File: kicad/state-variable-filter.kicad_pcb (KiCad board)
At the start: 2 copper layers, 0 parts

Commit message: Updating hardware design
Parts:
- added C1: 10nF, Rumblesan_Standard_Parts:C_Rect_L7.0mm_W2.5mm_P5.00mm, F.Cu at (127.6, 58.7)
- added C10: 100nF, Rumblesan_Standard_Parts:C_Rect_L7.0mm_W2.5mm_P5.00mm, F.Cu at (154.4, 52.8)
- added C11: 22pF, Rumblesan_Standard_Parts:C_Rect_L7.0mm_W2.5mm_P5.00mm, F.Cu at (140.2, 58.7)
- added C12: 220pF, Capacitor_THT:C_Rect_L7.0mm_W4.5mm_P5.00mm, F.Cu at (152.7, 88.4)
- added C13: 100nF, Rumblesan_Standard_Parts:C_Rect_L7.0mm_W2.5mm_P5.00mm, F.Cu at (151.4, 85.3)
- added C14: 22pF, Rumblesan_Standard_Parts:C_Rect_L7.0mm_W2.5mm_P5.00mm, F.Cu at (156.7, 71.6)
- added C15: 560pF, Rumblesan_Standard_Parts:C_Rect_L7.0mm_W2.5mm_P5.00mm, F.Cu at (161.5, 97.3)
- added C16: 100nF, Rumblesan_Standard_Parts:C_Rect_L7.0mm_W2.5mm_P5.00mm, F.Cu at (151.4, 134.4)
- added C17: 560pF, Rumblesan_Standard_Parts:C_Rect_L7.0mm_W2.5mm_P5.00mm, F.Cu at (161.0, 117.3)
- added C18: 22pF, Rumblesan_Standard_Parts:C_Rect_L7.0mm_W2.5mm_P5.00mm, F.Cu at (164.1, 126.2)
- added C19: 10uF, Rumblesan_Standard_Parts:CP_Radial_D5.0mm_P2.00mm, B.Cu at (162.6, 153.4)
- added C2: 100nF, Rumblesan_Standard_Parts:C_Rect_L7.0mm_W2.5mm_P5.00mm, F.Cu at (135.2, 61.7)
- added C20: 10uF, Rumblesan_Standard_Parts:CP_Radial_D5.0mm_P2.00mm, B.Cu at (123.2, 153.4)
- added C3: 100nF, Rumblesan_Standard_Parts:C_Rect_L7.0mm_W2.5mm_P5.00mm, F.Cu at (132.2, 85.3)
- added C4: 220pF, Capacitor_THT:C_Rect_L7.0mm_W4.5mm_P5.00mm, F.Cu at (135.9, 88.4)
- added C5: 560pF, Rumblesan_Standard_Parts:C_Rect_L7.0mm_W2.5mm_P5.00mm, F.Cu at (133.9, 106.9)
- added C6: 100nF, Rumblesan_Standard_Parts:C_Rect_L7.0mm_W2.5mm_P5.00mm, F.Cu at (132.2, 101.9)
- added C7: 100nF, Rumblesan_Standard_Parts:C_Rect_L7.0mm_W2.5mm_P5.00mm, F.Cu at (137.2, 120.1)
- added C8: 100nF, Rumblesan_Standard_Parts:C_Rect_L7.0mm_W2.5mm_P5.00mm, F.Cu at (132.2, 135.9)
- added C9: 20pF, Rumblesan_Standard_Parts:C_Rect_L7.0mm_W2.5mm_P5.00mm, F.Cu at (122.3, 132.8)
- added D1: 1N4148, Rumblesan_Standard_Parts:D_DO-35_SOD27_P7.62mm_Horizontal, F.Cu at (132.8, 61.5)
- added D10: 1N4148, Rumblesan_Standard_Parts:D_DO-35_SOD27_P7.62mm_Horizontal, F.Cu at (151.1, 128.5)
- added D11: 1N5818, Rumblesan_Standard_Parts:D_DO-41_SOD81_P10.16mm_Horizontal, F.Cu at (157.0, 147.6)
- added D2: 1N4148, Rumblesan_Standard_Parts:D_DO-35_SOD27_P7.62mm_Horizontal, F.Cu at (133.6, 67.6)
- added D3: 1n4148, Rumblesan_Standard_Parts:D_DO-35_SOD27_P7.62mm_Horizontal, F.Cu at (129.8, 133.1)
- added D4: 1n4148, Rumblesan_Standard_Parts:D_DO-35_SOD27_P7.62mm_Horizontal, F.Cu at (129.8, 136.1)
- added D5: 1N5818, Rumblesan_Standard_Parts:D_DO-41_SOD81_P10.16mm_Horizontal, F.Cu at (129.0, 157.7)
- added D6: 1N4148, Rumblesan_Standard_Parts:D_DO-35_SOD27_P7.62mm_Horizontal, F.Cu at (140.5, 55.9)
- added D7: 6v8, Rumblesan_Standard_Parts:D_DO-35_SOD27_P7.62mm_Horizontal, F.Cu at (161.3, 108.5)
- added D8: 6v8, Rumblesan_Standard_Parts:D_DO-35_SOD27_P7.62mm_Horizontal, F.Cu at (158.8, 98.3)
- added D9: 1N4148, Rumblesan_Standard_Parts:D_DO-35_SOD27_P7.62mm_Horizontal, F.Cu at (158.8, 126.0)
- added J1: AudioJack2_SwitchT, Rumblesan_Audio_Connectors:Jack_3.5mm_QingPu_WQP-PJ398SM_Vertical, F.Cu at (81.5, 58.0)
- added J10: AudioJack2_SwitchT, Rumblesan_Audio_Connectors:Jack_3.5mm_QingPu_WQP-PJ398SM_Vertical, F.Cu at (107.5, 119.0)
- added J11: AudioJack2_SwitchT, Rumblesan_Audio_Connectors:Jack_3.5mm_QingPu_WQP-PJ398SM_Vertical, F.Cu at (94.5, 119.0)
- added J12: Conn_01x08_Pin, Connector_PinHeader_2.54mm:PinHeader_1x08_P2.54mm_Vertical, F.Cu at (122.4, 102.0)
- added J13: Conn_01x08_Socket, Connector_PinSocket_2.54mm:PinSocket_1x08_P2.54mm_Vertical, F.Cu at (116.6, 102.0)
- added J14: Conn_01x08_Pin, Connector_PinHeader_2.54mm:PinHeader_1x08_P2.54mm_Vertical, F.Cu at (166.6, 102.0)
- added J15: Conn_02x05_Odd_Even, Rumblesan_Eurorack_Power:Eurorack_Power_IDC-Header_2x05_P2.54mm_Vertical, B.Cu at (139.2, 151.6)
- added J2: Conn_01x08_Socket, Connector_PinSocket_2.54mm:PinSocket_1x08_P2.54mm_Vertical, F.Cu at (72.4, 102.0)
- added J3: AudioJack2_SwitchT, Rumblesan_Audio_Connectors:Jack_3.5mm_QingPu_WQP-PJ398SM_Vertical, F.Cu at (81.5, 102.0)
- added J4: AudioJack2_SwitchT, Rumblesan_Audio_Connectors:Jack_3.5mm_QingPu_WQP-PJ398SM_Vertical, F.Cu at (81.5, 119.0)
- added J5: AudioJack2_SwitchT, Rumblesan_Audio_Connectors:Jack_3.5mm_QingPu_WQP-PJ398SM_Vertical, F.Cu at (94.5, 58.0)
- added J6: AudioJack2_SwitchT, Rumblesan_Audio_Connectors:Jack_3.5mm_QingPu_WQP-PJ398SM_Vertical, F.Cu at (107.5, 58.0)
- added J7: AudioJack2_SwitchT, Rumblesan_Audio_Connectors:Jack_3.5mm_QingPu_WQP-PJ398SM_Vertical, F.Cu at (94.5, 74.0)
- added J8: AudioJack2_SwitchT, Rumblesan_Audio_Connectors:Jack_3.5mm_QingPu_WQP-PJ398SM_Vertical, F.Cu at (94.5, 102.0)
- added J9: AudioJack2_SwitchT, Rumblesan_Audio_Connectors:Jack_3.5mm_QingPu_WQP-PJ398SM_Vertical, F.Cu at (107.5, 102.0)
- added JP1: Jumper_2_Open, Connector_PinHeader_2.54mm:PinHeader_1x02_P2.54mm_Vertical, B.Cu at (159.8, 85.6)
- added JP2: Jumper_2_Open, Connector_PinHeader_2.54mm:PinHeader_1x02_P2.54mm_Vertical, B.Cu at (135.1, 123.4)
- added NT1: NetTie_2, NetTie:NetTie-2_SMD_Pad0.5mm, F.Cu at (124.7, 146.3)
- added R1: 330r, Rumblesan_Standard_Parts:R_Axial_DIN0207_L6.3mm_D2.5mm_P10.16mm_Horizontal, F.Cu at (86.6, 69.5)
- added R10: 330k, Rumblesan_Standard_Parts:R_Axial_DIN0207_L6.3mm_D2.5mm_P10.16mm_Horizontal, F.Cu at (125.2, 64.8)
- added R11: 33k, Rumblesan_Standard_Parts:R_Axial_DIN0207_L6.3mm_D2.5mm_P10.16mm_Horizontal, F.Cu at (138.7, 98.0)
- added R12: 100k, Rumblesan_Standard_Parts:R_Axial_DIN0207_L6.3mm_D2.5mm_P10.16mm_Horizontal, F.Cu at (137.4, 126.7)
- added R13: 33k, Rumblesan_Standard_Parts:R_Axial_DIN0207_L6.3mm_D2.5mm_P10.16mm_Horizontal, F.Cu at (137.4, 129.8)
- added R14: 33k, Rumblesan_Standard_Parts:R_Axial_DIN0207_L6.3mm_D2.5mm_P10.16mm_Horizontal, F.Cu at (132.3, 138.9)
- added R15: 510r, Rumblesan_Standard_Parts:R_Axial_DIN0207_L6.3mm_D2.5mm_P10.16mm_Horizontal, F.Cu at (136.9, 117.1)
- added R16: 33k, Rumblesan_Standard_Parts:R_Axial_DIN0207_L6.3mm_D2.5mm_P10.16mm_Horizontal, F.Cu at (137.4, 142.0)
- added R17: 33k, Rumblesan_Standard_Parts:R_Axial_DIN0207_L6.3mm_D2.5mm_P10.16mm_Horizontal, F.Cu at (154.2, 55.9)
- added R18: 33k, Rumblesan_Standard_Parts:R_Axial_DIN0207_L6.3mm_D2.5mm_P10.16mm_Horizontal, F.Cu at (154.2, 58.9)
- added R19: 100k, Rumblesan_Standard_Parts:R_Axial_DIN0207_L6.3mm_D2.5mm_P10.16mm_Horizontal, F.Cu at (162.8, 66.5)
- added R2: 330r, Rumblesan_Standard_Parts:R_Axial_DIN0207_L6.3mm_D2.5mm_P10.16mm_Horizontal, F.Cu at (86.6, 72.6)
- added R20: 100k, Rumblesan_Standard_Parts:R_Axial_DIN0207_L6.3mm_D2.5mm_P10.16mm_Horizontal, F.Cu at (140.5, 74.2)
- added R21: 100k, Rumblesan_Standard_Parts:R_Axial_DIN0207_L6.3mm_D2.5mm_P10.16mm_Horizontal, F.Cu at (161.3, 81.0)
- added R22: 220k, Rumblesan_Standard_Parts:R_Axial_DIN0207_L6.3mm_D2.5mm_P10.16mm_Horizontal, F.Cu at (150.6, 65.0)
- added R23: 330k, Rumblesan_Standard_Parts:R_Axial_DIN0207_L6.3mm_D2.5mm_P10.16mm_Horizontal, F.Cu at (159.8, 76.7)
- added R24: 100k, Rumblesan_Standard_Parts:R_Axial_DIN0207_L6.3mm_D2.5mm_P10.16mm_Horizontal, F.Cu at (140.5, 71.1)
- added R25: 33k, Rumblesan_Standard_Parts:R_Axial_DIN0207_L6.3mm_D2.5mm_P10.16mm_Horizontal, F.Cu at (150.6, 68.1)
- added R26: 510r, Rumblesan_Standard_Parts:R_Axial_DIN0207_L6.3mm_D2.5mm_P10.16mm_Horizontal, F.Cu at (151.1, 114.3)
- added R27: 510r, Rumblesan_Standard_Parts:R_Axial_DIN0207_L6.3mm_D2.5mm_P10.16mm_Horizontal, F.Cu at (151.1, 102.6)
- added R28: 33k, Rumblesan_Standard_Parts:R_Axial_DIN0207_L6.3mm_D2.5mm_P10.16mm_Horizontal, F.Cu at (151.1, 105.7)
- added R29: 33k, Rumblesan_Standard_Parts:R_Axial_DIN0207_L6.3mm_D2.5mm_P10.16mm_Horizontal, F.Cu at (151.1, 111.3)
- added R3: 330r, Rumblesan_Standard_Parts:R_Axial_DIN0207_L6.3mm_D2.5mm_P10.16mm_Horizontal, F.Cu at (102.4, 72.6)
- added R30: 33k, Rumblesan_Standard_Parts:R_Axial_DIN0207_L6.3mm_D2.5mm_P10.16mm_Horizontal, F.Cu at (161.3, 131.3)
- added R31: 100k, Rumblesan_Standard_Parts:R_Axial_DIN0207_L6.3mm_D2.5mm_P10.16mm_Horizontal, F.Cu at (151.1, 137.4)
- added R32: 33k, Rumblesan_Standard_Parts:R_Axial_DIN0207_L6.3mm_D2.5mm_P10.16mm_Horizontal, F.Cu at (161.3, 143.5)
- added R33: 100k, Rumblesan_Standard_Parts:R_Axial_DIN0207_L6.3mm_D2.5mm_P10.16mm_Horizontal, F.Cu at (164.1, 143.8)
- added R34: 33k, Rumblesan_Standard_Parts:R_Axial_DIN0207_L6.3mm_D2.5mm_P10.16mm_Horizontal, F.Cu at (161.3, 140.5)
- added R35: 100k, Rumblesan_Standard_Parts:R_Axial_DIN0207_L6.3mm_D2.5mm_P10.16mm_Horizontal, F.Cu at (165.9, 66.5)
- added R36: 100k, Rumblesan_Standard_Parts:R_Axial_DIN0207_L6.3mm_D2.5mm_P10.16mm_Horizontal, F.Cu at (150.9, 123.2)
- added R4: 330r, Rumblesan_Standard_Parts:R_Axial_DIN0207_L6.3mm_D2.5mm_P10.16mm_Horizontal, F.Cu at (102.4, 69.5)
- added R5: 100k, Rumblesan_Standard_Parts:R_Axial_DIN0207_L6.3mm_D2.5mm_P10.16mm_Horizontal, F.Cu at (90.4, 141.5)
- added R6: 100k, Rumblesan_Standard_Parts:R_Axial_DIN0207_L6.3mm_D2.5mm_P10.16mm_Horizontal, F.Cu at (98.5, 141.5)
- added R7: 180k, Rumblesan_Standard_Parts:R_Axial_DIN0207_L6.3mm_D2.5mm_P10.16mm_Horizontal, F.Cu at (122.2, 55.6)
- added R8: 1M5, Rumblesan_Standard_Parts:R_Axial_DIN0207_L6.3mm_D2.5mm_P10.16mm_Horizontal, F.Cu at (130.3, 53.1)
- added R9: 100k, Rumblesan_Standard_Parts:R_Axial_DIN0207_L6.3mm_D2.5mm_P10.16mm_Horizontal, F.Cu at (127.3, 80.3)
- added RV1: 10kA, Rumblesan_Potentiometer_THT:Potentiometer_Alpha_RD901F-40-00D_Single_Vertical, F.Cu at (81.5, 83.0)
- added RV2: 10k, Rumblesan_Potentiometer_THT:Potentiometer_Alpha_RD901F-40-00D_Single_Vertical, F.Cu at (81.5, 134.0)
- added RV3: 10k, Rumblesan_Potentiometer_THT:Potentiometer_Alpha_RD901F-40-00D_Single_Vertical, F.Cu at (81.5, 150.0)
- added RV4: 10kA, Rumblesan_Potentiometer_THT:Potentiometer_Alpha_RD901F-40-00D_Single_Vertical, F.Cu at (107.5, 83.0)
- added RV5: 10kB, Rumblesan_Potentiometer_THT:Potentiometer_Alpha_RD901F-40-00D_Single_Vertical, F.Cu at (107.5, 134.0)
- added RV6: 10k, Rumblesan_Potentiometer_THT:Potentiometer_Alpha_RD901F-40-00D_Single_Vertical, F.Cu at (107.5, 150.0)
- added RV7: 2k, Rumblesan_Potentiometer_THT:Potentiometer_Vishay_T93YB_Vertical, B.Cu at (160.0, 123.2)
- added TP1: TestPoint, Rumblesan_Standard_Parts:TestPoint_Loop_D2.50mm_Drill1.0mm_LowProfile, B.Cu at (159.5, 134.4)
- added TP2: TestPoint, Rumblesan_Standard_Parts:TestPoint_Loop_D2.50mm_Drill1.0mm_LowProfile, B.Cu at (127.3, 83.8)
- added TP3: TestPoint, Rumblesan_Standard_Parts:TestPoint_Loop_D2.50mm_Drill1.0mm_LowProfile, B.Cu at (132.8, 71.6)
- added TP4: TestPoint, Rumblesan_Standard_Parts:TestPoint_Loop_D2.50mm_Drill1.0mm_LowProfile, B.Cu at (131.1, 115.1)
- added U1: TL072, Package_DIP:DIP-8_W7.62mm_Socket, F.Cu at (143.5, 53.3)
- added U2: TL074, Package_DIP:DIP-14_W7.62mm_Socket, F.Cu at (148.1, 93.0)
- added U3: SSI2164, Package_DIP:DIP-16_W7.62mm_Socket, F.Cu at (148.1, 119.6)
- added U4: TL074, Package_DIP:DIP-14_W7.62mm_Socket, F.Cu at (148.1, 142.5)
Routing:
- net VCC: track 0.00 -> 142.3 mm, vias 0 -> 1
- net VEE: track 0.00 -> 132.7 mm
- net NOTCH_OUTPUT: track 0.00 -> 91.6 mm
- net HI_PASS_OUTPUT: track 0.00 -> 77.0 mm
- net /NEG_VREF_CTRL: track 0.00 -> 70.7 mm
- net LOW_PASS_OUTPUT: track 0.00 -> 61.6 mm
- net /RES_ATTV_CW_MAIN: track 0.00 -> 56.8 mm
- net /FREQ_ATTV_CW_MAIN: track 0.00 -> 52.8 mm
- net Net-(U2C--): track 0.00 -> 49.2 mm
- net /PING_MAIN: track 0.00 -> 49.1 mm
- net /RES_CV_CTRL: track 0.00 -> 48.8 mm
- net /FREQ_CV_CTRL: track 0.00 -> 46.1 mm
- net /FREQ_ATTV_ACW_MAIN: track 0.00 -> 45.5 mm
- net Net-(U2B--): track 0.00 -> 43.9 mm
- net /FILTER_INPUT_2_CTRL: track 0.00 -> 43.5 mm
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- added copper zone on B.Cu, net GND
- added copper zone on F.Cu, net GND
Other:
- board outline added: 99 x 110 mm
- board text added: "Freq to Res"
- board text added: "Oscilate Helper"

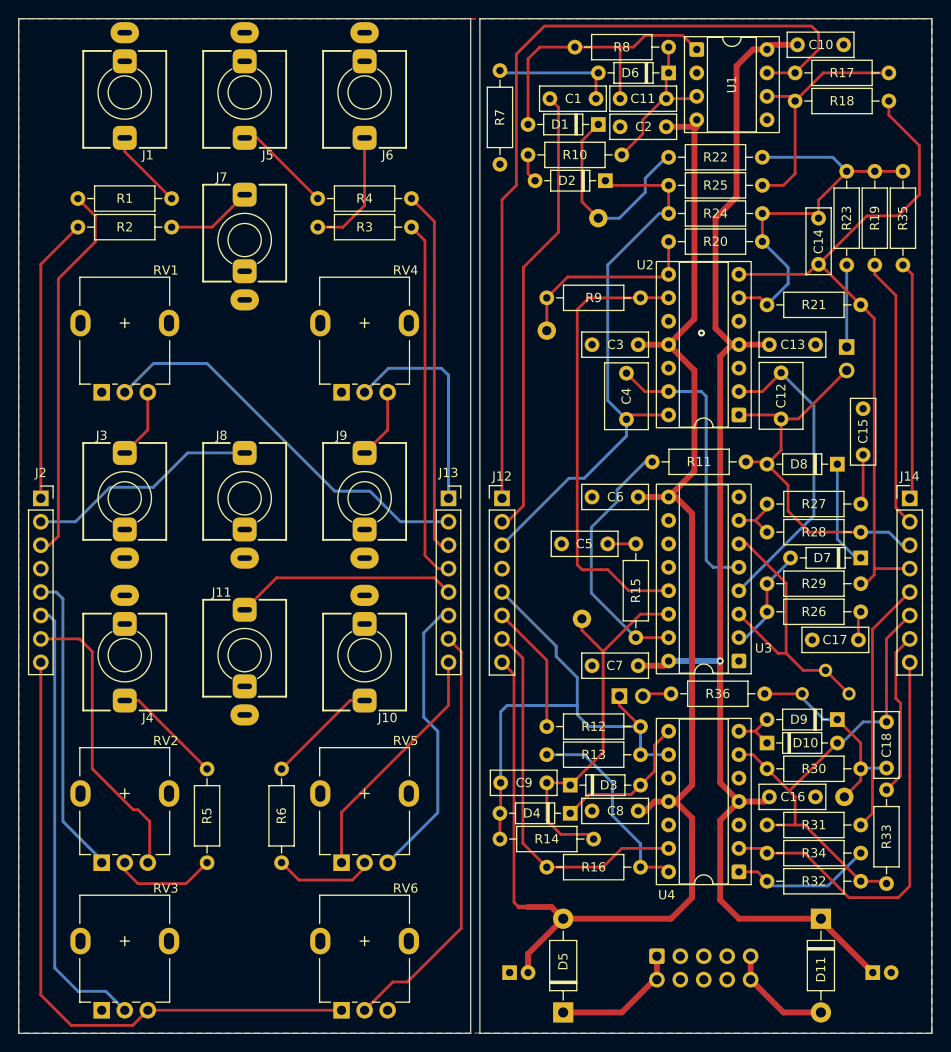
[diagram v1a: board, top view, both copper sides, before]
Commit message: Updating design
* Adding resonance control curve jumper
* improving layout
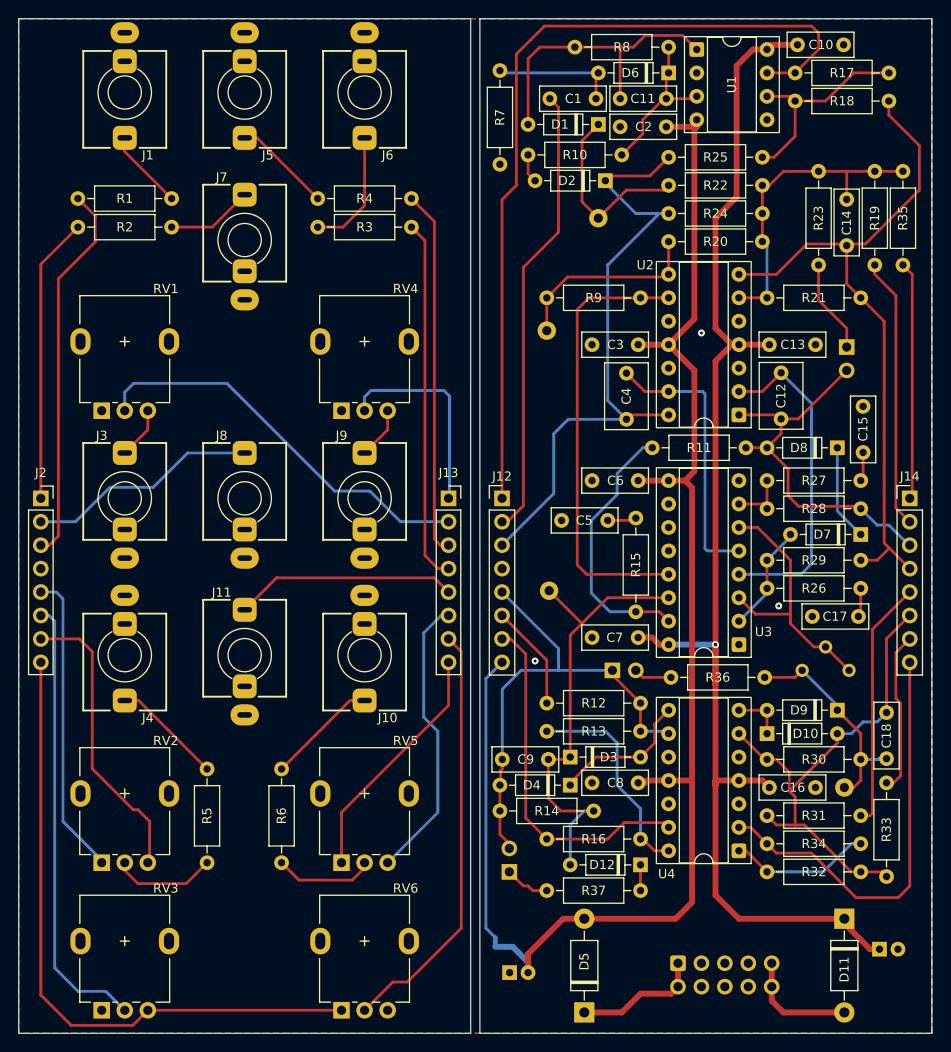
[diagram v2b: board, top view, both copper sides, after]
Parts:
- added D12: 1n4148, Rumblesan_Standard_Parts:D_DO-35_SOD27_P7.62mm_Horizontal, F.Cu at (137.4, 141.7)
- added JP3: Jumper_2_Open, Connector_PinHeader_2.54mm:PinHeader_1x02_P2.54mm_Vertical, B.Cu at (123.2, 142.5)
- added R37: 33k, Rumblesan_Standard_Parts:R_Axial_DIN0207_L6.3mm_D2.5mm_P10.16mm_Horizontal, F.Cu at (137.4, 144.5)
- NT1: moved to B.Cu
- moved NT1 4.87 mm to (121.7, 150.1), turned to -90 degrees
- moved TP4 4.68 mm to (127.5, 112.0)
- moved C14 3.66 mm to (159.8, 69.6)
- moved C7 3.05 mm to (137.2, 117.1)
- moved D3 3.05 mm to (129.8, 130.0)
- moved D4 3.05 mm to (129.8, 133.1)
- moved R14 3.05 mm to (132.3, 135.9)
- moved R16 3.05 mm to (137.4, 138.9)
- moved R22 3.05 mm to (150.6, 68.1)
- moved R23 3.05 mm to (156.7, 76.7)
- moved R25 3.05 mm to (150.6, 65.0)
- moved C8 3.05 mm to (132.2, 132.8)
- moved JP2 2.90 mm to (134.4, 120.7)
- moved R15 2.79 mm to (136.9, 114.3)
- moved C19 2.64 mm to (163.3, 150.9)
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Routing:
- net Net-(U2B--): track 43.9 -> 34.4 mm
- net LOW_PASS_OUTPUT: track 61.6 -> 70.6 mm
- net RES_VC: track 41.9 -> 50.3 mm
- net Net-(JP3-A): track 0.00 -> 4.91 mm
- net /RES_ATTV_CW_MAIN: track 56.8 -> 52.6 mm
- net /NEG_VREF_MAIN: track 27.3 -> 31.0 mm
- net Net-(U1B--): track 26.6 -> 23.0 mm
- net Net-(D12-K): track 0.00 -> 2.79 mm
- net VCC: track 142.3 -> 144.9 mm
- net /RES_CV_MAIN: track 14.1 -> 11.5 mm
- net /RES_ATTV_ACW_MAIN: track 40.9 -> 38.4 mm
- net Net-(C15-Pad1): track 5.44 -> 3.15 mm
- net /FREQ_ATTV_CW_MAIN: track 52.8 -> 55.1 mm
- net Net-(D1-K): track 22.9 -> 20.7 mm
- net Net-(J9-PadT): track 7.62 -> 5.62 mm
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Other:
- board text added: "Oscillate helper"
- board text added: "Res ctrl curve"
- board text added: "V/oct"
- board text removed: "Oscilate Helper"

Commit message: Fixing a couple issues with schematic and layout
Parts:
- added H1: MountingHole_Pad, Rumblesan_Standard_Parts:MountingHole_3.2mm_M3_DIN965_Pad, F.Cu at (129.5, 76.0)
- added H2: MountingHole_Pad, Rumblesan_Standard_Parts:MountingHole_3.2mm_M3_DIN965_Pad, F.Cu at (79.5, 76.0)
- added H3: MountingHole_Pad, Rumblesan_Standard_Parts:MountingHole_3.2mm_M3_DIN965_Pad, F.Cu at (94.2, 145.2)
- added H4: MountingHole_Pad, Rumblesan_Standard_Parts:MountingHole_3.2mm_M3_DIN965_Pad, F.Cu at (144.2, 145.2)
- added mouse-bite-1mm-slot: VAL**, Rumblesan_Panelization:mouse-bite-1mm-slot, F.Cu at (119.5, 60.0)
- added mouse-bite-1mm-slot: VAL**, Rumblesan_Panelization:mouse-bite-1mm-slot, F.Cu at (119.5, 124.0)
- added mouse-bite-1mm-slot: VAL**, Rumblesan_Panelization:mouse-bite-1mm-slot, F.Cu at (119.5, 140.0)
- added mouse-bite-1mm-slot: VAL**, Rumblesan_Panelization:mouse-bite-1mm-slot, F.Cu at (119.5, 150.0)
- added mouse-bite-1mm-slot: VAL**, Rumblesan_Panelization:mouse-bite-1mm-slot, F.Cu at (119.5, 98.0)
- added mouse-bite-1mm-slot: VAL**, Rumblesan_Panelization:mouse-bite-1mm-slot, F.Cu at (119.5, 80.0)
- J13, J2: moved to B.Cu
- moved R7 7.80 mm to (122.0, 63.4)
- moved R2 1.75 mm to (86.4, 70.9)
- moved R1 1.70 mm to (86.4, 67.8)
- moved NT1 1.16 mm to (122.0, 149.0)
- moved TP3 1.10 mm to (133.5, 70.8)
- moved TP2 0.68 mm to (127.2, 84.5)
- moved R9 0.49 mm to (127.2, 80.8)
- turned J13 to 180 degrees
- turned J2 to 180 degrees
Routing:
- net Net-(D6-A): track 13.7 -> 20.9 mm
- net VCC: track 144.9 -> 142.2 mm
- net VEE: track 133.1 -> 130.7 mm
- net /LOWPASS_CTRL: track 41.3 -> 43.1 mm
- net /NOTCH_CTRL: track 31.1 -> 32.7 mm
- net /NEG_VREF_MAIN: track 31.0 -> 30.0 mm
- net Net-(J1-PadT): track 8.68 -> 7.77 mm
- net Net-(D1-K): track 20.7 -> 20.0 mm
- net Net-(U2C--): track 48.4 -> 47.8 mm
- net Net-(R20-Pad1): track 21.4 -> 21.9 mm
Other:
- outline, holes or cut-outs redrawn
